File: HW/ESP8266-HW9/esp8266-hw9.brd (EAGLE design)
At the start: 58 x 52 mm, 31 parts, among them IC1 MCP1703CB, IC2 ATECC608A-SSHDA-B, IC3 DS18B20U+, J2 Sensors2, J3 Analog, J4 Sensors1, J5 Enable, J6 PGM, J9 Pwr sw, T1 BSS138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

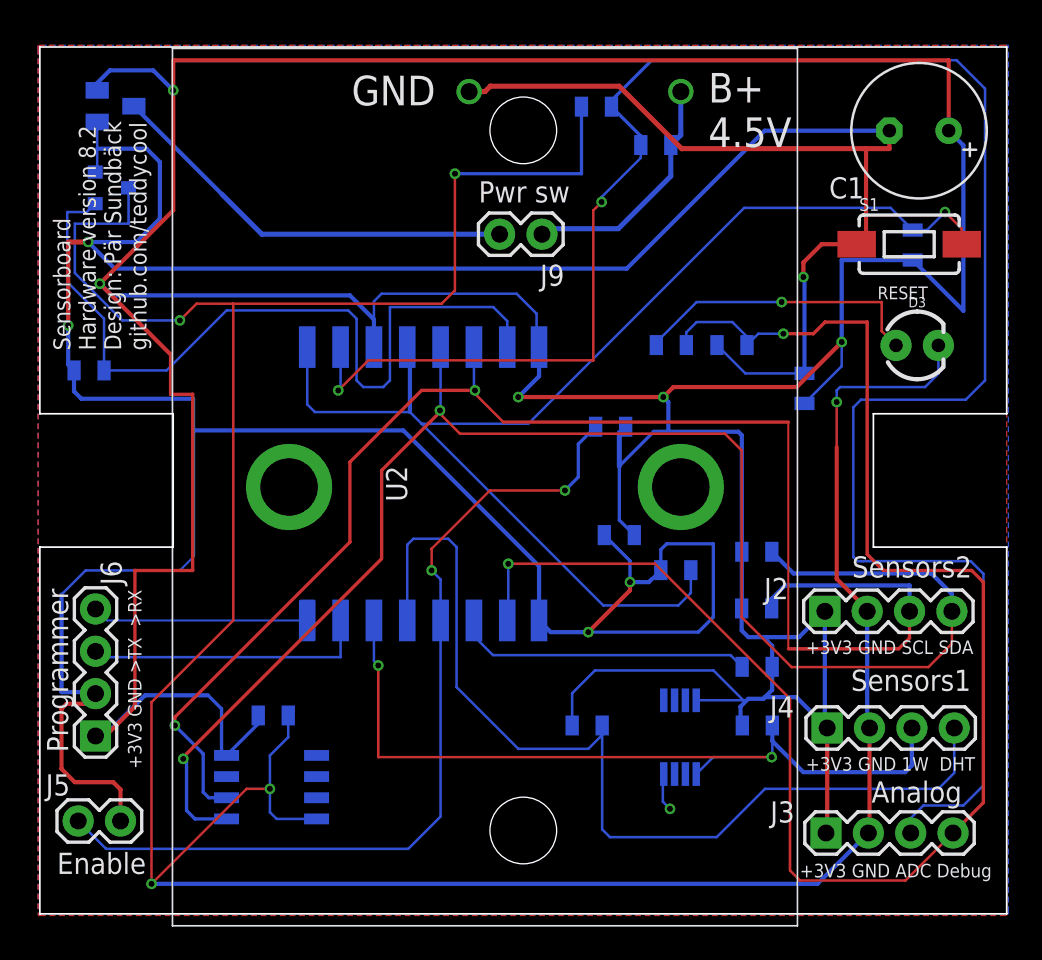
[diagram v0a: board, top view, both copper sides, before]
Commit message: New pcb releases and some updated software
New (final?) releases of pcbs for version 7 and 8. New test program to run for test of the built hardware.
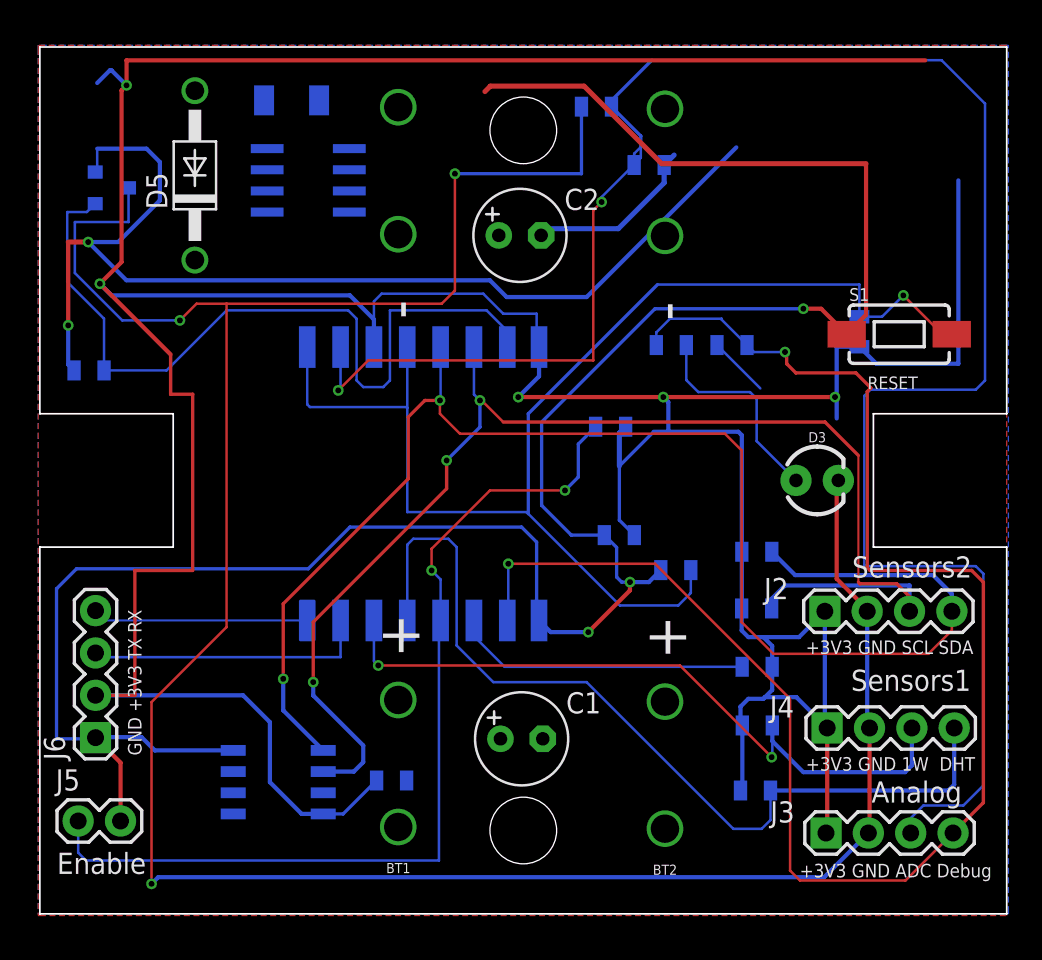
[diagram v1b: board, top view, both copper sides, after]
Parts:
- removed IC1: MCP1703CB, linear:SOT23
- removed IC3: DS18B20U+, SamacSys_Parts:SOP65P490X110-8N
- removed J9: Pwr sw, SparkFun-Connectors:1X02
- added BT1, BT2: (no value), SparkFun-Batteries:BATTERY-AAA
- added D5: 1N5817, diode:DO41-10
- added L1: 47uH, inductor-neosid:SM-1206
- C1: value 1000uF -> 68uF; device rcl:E3,5-8 -> resistor:E2,5-6
- C2: value 100nF -> 68uF; device SparkFun-Passives:0805 -> resistor:E2,5-6
- U2: value 2479 -> MAX856ESA+; device SamacSys_Parts:2479 -> max856:21-0041B_8
- moved C1 43.6 mm to (28.9, 10.5), turned to 0 degrees
- moved U2 21.2 mm to (16.1, 44.0), flipped to the bottom, turned to 0 degrees
- moved C2 19.4 mm to (28.8, 40.7), flipped to the top, turned to 0 degrees
- moved R3 10.8 mm to (42.9, 7.40)
- moved D3 10.1 mm to (46.6, 26.0)
- moved C5 8.10 mm to (21.1, 8.00)
- moved R4 6.11 mm to (49.2, 34.9)
- moved S1 5.43 mm to (51.5, 34.8)
- moved R5 1.26 mm to (36.5, 44.9)
- moved IC2 0.50 mm to (14.3, 7.90), turned to 180 degrees
- moved J6 0.10 mm to (3.34, 10.6)
- turned R14 to 0 degrees
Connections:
- removed net PWR: IC1.3, J9.2
- new net LX: L1.2
- new net N$1: D5.A, U2.8
- new net N$2: U2.6
- net +3V3: now also D5.C, J6.2; no longer C1.+, C2.1, IC1.2, IC3.8, J6.1
- net 1W: no longer IC3.1
- net B+: now also BT1.PWR@1, BT2.PWR@1, C1.+, L1.1, U2.5; no longer J9.1, U2.1
- net GND: now also BT1.GND@1, BT2.GND@1, C2.-, C5.2, IC2.4, J6.1, U2.7; no longer C2.2, IC1.1, J6.2, U2.2
- net SPW: no longer C5.2, IC2.4, IC3.4
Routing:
- net SPW: track 189.3 -> 154.6 mm, vias 6 -> 3
- net PWR: track 25.1 -> 0.00 mm
- net +3V3: track 286.0 -> 264.4 mm
- net GND: track 230.8 -> 211.0 mm
- net SCL: track 91.5 -> 79.8 mm, vias 2 -> 3
- net 1W: track 50.3 -> 42.2 mm
- net SDA: track 95.4 -> 87.8 mm
- net DHT: track 58.7 -> 53.7 mm
- net N$8: track 17.6 -> 12.7 mm, vias 1 -> 0
- net B+: track 14.5 -> 10.1 mm
- net PGM: track 53.6 -> 56.7 mm
- net RST: track 77.2 -> 78.5 mm
- net SPC: track 48.5 -> 47.9 mm
- net GPIO15: track 95.9 -> 95.3 mm
- added copper zone on layer 1, net GND
- removed copper zone on layer 1, net SPW
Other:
- board text added: "GND +3V3 TX RX"
- board text removed: "+3V3 GND >TX >RX"
- board text removed: "B+ 4.5V"
- board text removed: "B+ 4.5V 3xAAA"
- board text removed: "GND"
- board text removed: "HSM"
- board text removed: "Programmer"
- board text removed: "Sensorboard Hardware version 8.2 Design: Pär Sundbäck github.com/teddycool"
- board text removed: "Temp"
